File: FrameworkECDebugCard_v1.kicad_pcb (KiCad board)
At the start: 2 copper layers, 26 x 30 mm, 25 parts, among them J1 Conn_01x05, P1 USB_C_Plug_USB2.0, P2 USB_B_Micro, U1 FT230XS

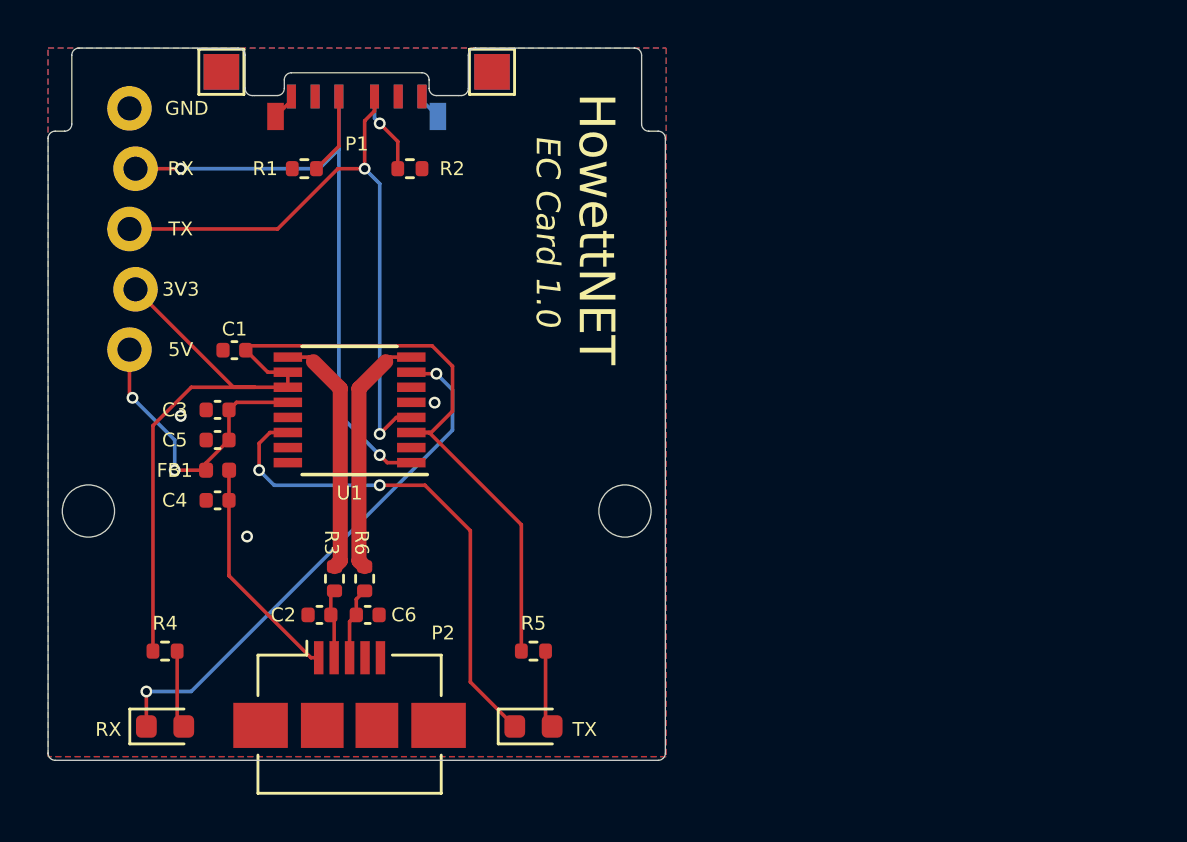
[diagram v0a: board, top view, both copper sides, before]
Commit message: Re-route everything to avoid B.Cu cuts across diff pair
Switched the positions of the TX and RX LEDs to match which side of the
chip they're on. Significantly re-routed TX/RX. Added via stitching.

The ground planes are much more contiguous, except for U1 pad 5 which
connects to GND on the back with a via.

(Kieran's suggestion was to remove the lines on the back that cut
horizontally across the differential pair; I don't know if having
RXLED's sink next to the diff pair will be a problem.)

Re-version the card to "EC Card 2"
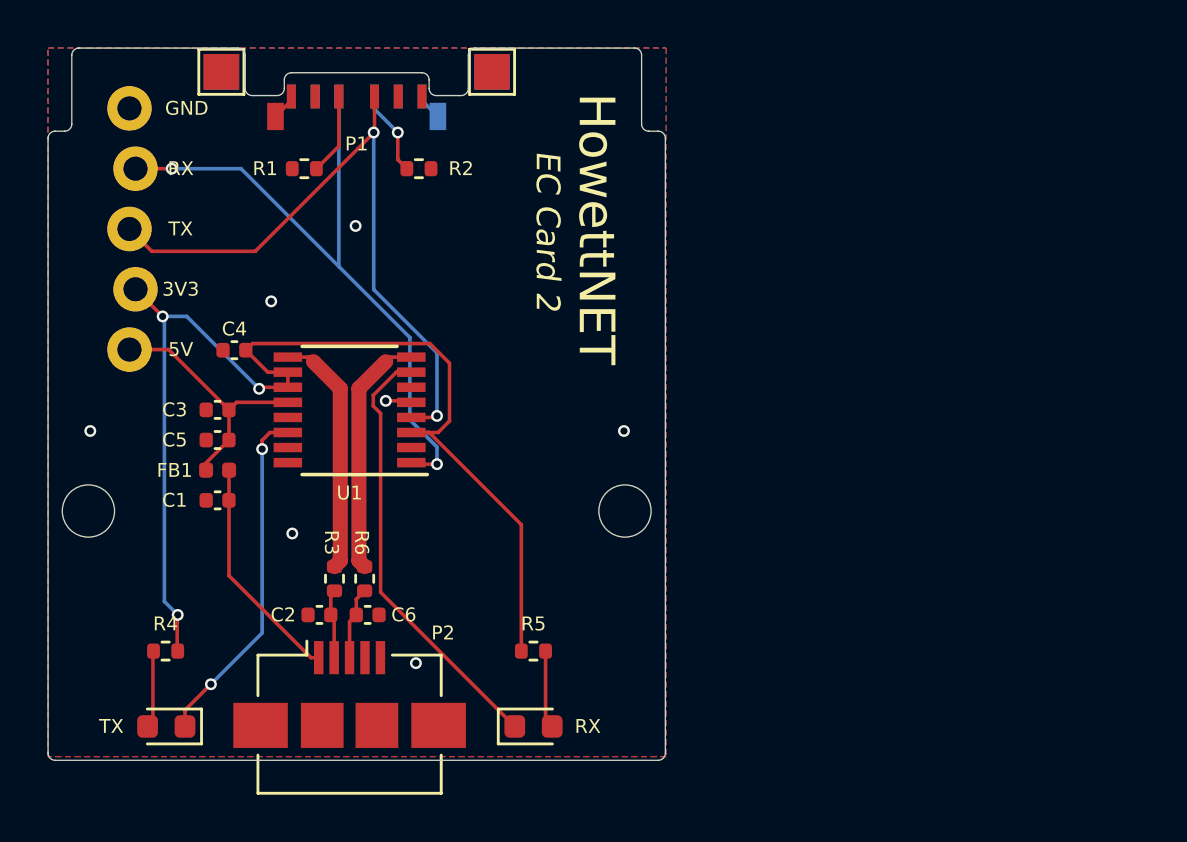
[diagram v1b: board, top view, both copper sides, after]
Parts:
- moved D2 15.5 mm to (147.4, 155.6)
- moved R5 15.5 mm to (147.4, 152.4)
- moved R4 15.5 mm to (132.0, 152.4), turned to 180 degrees
- moved D1 15.5 mm to (132.0, 155.6), turned to 180 degrees
- moved R2 0.38 mm to (142.6, 132.1)
- renumbered C4 to C1, C1 to C4, D2 to D1, D1 to D2, R5 to R4, R4 to R5
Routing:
- net /TXLED: track 21.5 -> 14.6 mm
- net /RXLED: track 22.7 -> 18.4 mm, vias 2 -> 0
- net /DIN: track 26.2 -> 28.6 mm
- net VBUS_HOST: track 12.7 -> 10.8 mm, vias 2 -> 0
- net /DOUT: track 27.2 -> 28.4 mm
- net GND: track 2.24 -> 3.34 mm, vias 3 -> 7
- net VCCIO: track 50.1 -> 50.2 mm, vias 0 -> 3
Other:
- board text added: "EC Card 2"
- board text removed: "EC Card 1.0"

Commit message: Add more stitching vias
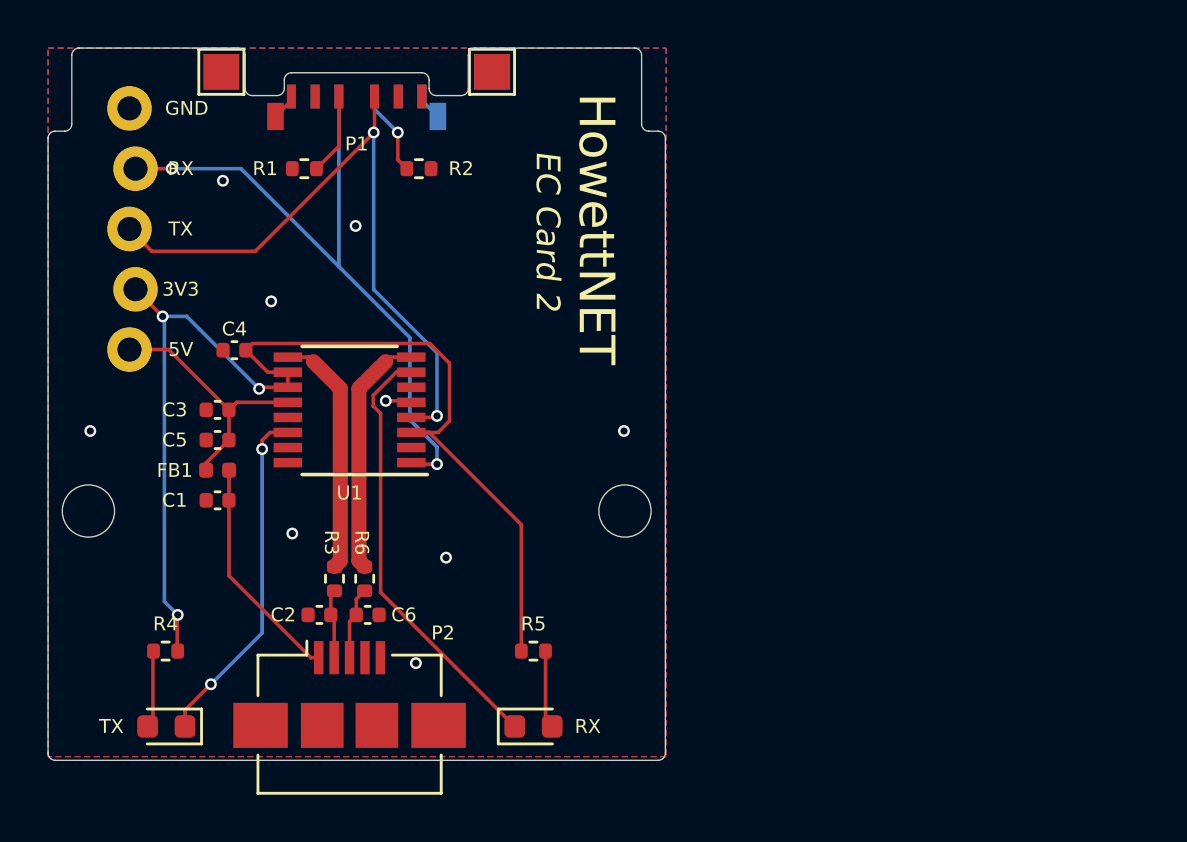
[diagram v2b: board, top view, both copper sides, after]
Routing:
- net GND: vias 7 -> 9
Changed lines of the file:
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@@
   (via (at 142.494 152.908) (size 0.5) (drill 0.3) (layers "F.Cu" "B.Cu") (free) (net 1))
   (via (at 128.778 143.129) (size 0.5) (drill 0.3) (layers "F.Cu" "B.Cu") (free) (net 1))
+  (via (at 134.366 132.588) (size 0.5) (drill 0.3) (layers "F.Cu" "B.Cu") (free) (net 1))
   (via (at 141.224 141.859) (size 0.5) (drill 0.3) (layers "F.Cu" "B.Cu") (free) (net 1))
+  (via (at 143.764 148.463) (size 0.5) (drill 0.3) (layers "F.Cu" "B.Cu") (free) (net 1))
   (via (at 139.954 134.493) (size 0.5) (drill 0.3) (layers "F.Cu" "B.Cu") (free) (net 1))
   (via (at 136.398 137.668) (size 0.5) (drill 0.3) (layers "F.Cu" "B.Cu") (free) (net 1))

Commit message: Update to KiCad 8, use narrower pads on USB C plug (PCBWay may mfg this)
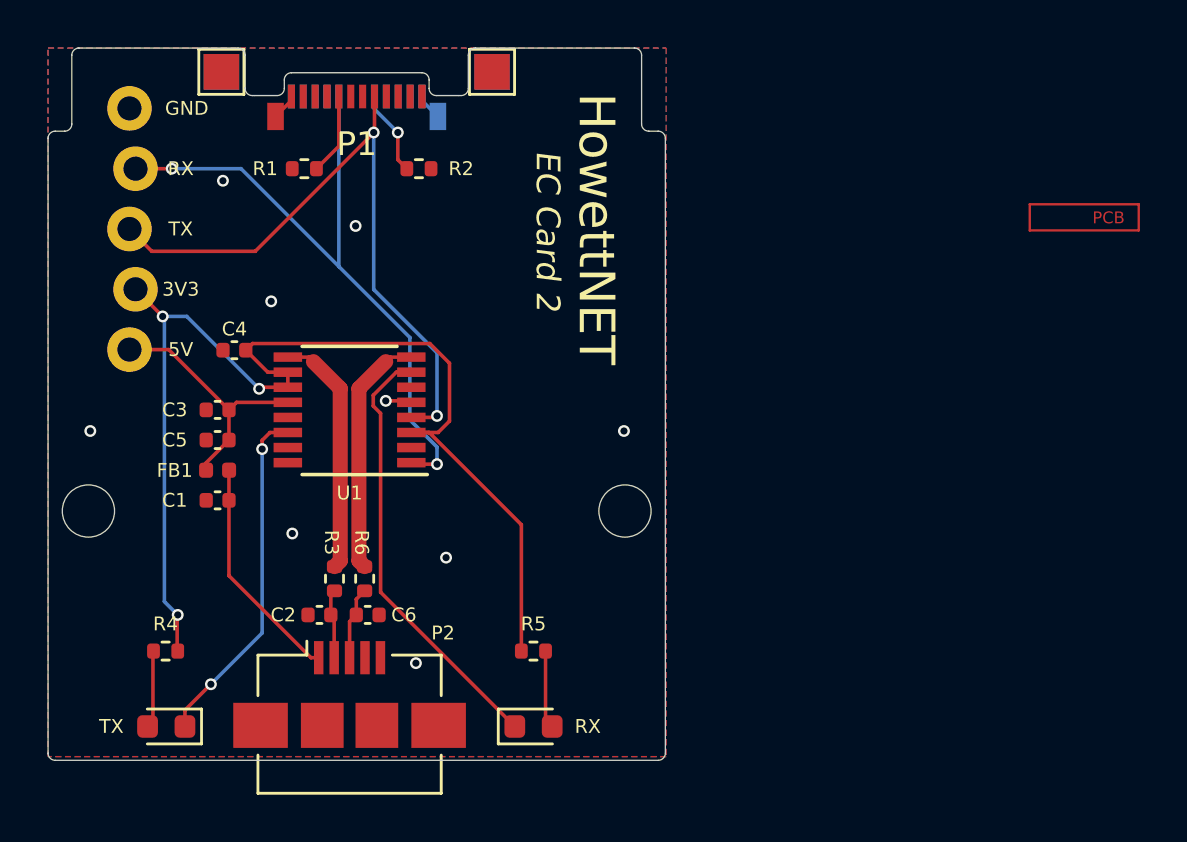
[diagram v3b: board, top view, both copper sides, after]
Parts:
- P1: footprint FrameworkECDebugCard_v1:USB_C_Plug_Molex_105444 -> FrameworkECDebugCard_v1:USB_C_Plug_Molex_105444_SmallPads
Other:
- board text added: "BOTTOM"
- board text added: "MOLEX 105444"
- board text added: "MOLEX 105444 1"
- board text added: "NC"
- board text added: "PCB"
- board text added: "TOP"

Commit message: ec card 3: recessed mid-mount usb c receptacle, fully rerouted
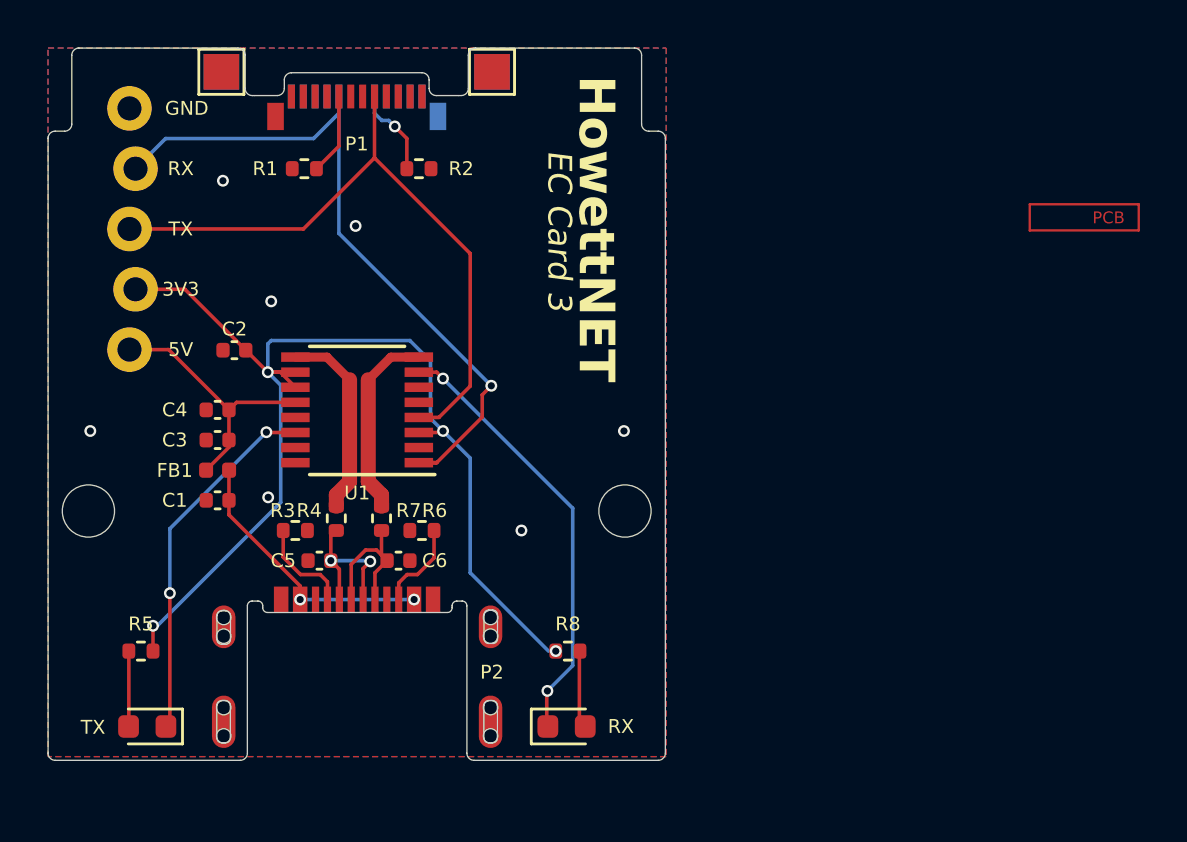
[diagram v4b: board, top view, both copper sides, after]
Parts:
- added ?: , , F.Cu at (145.6, 153.5)
- added R3: 5.1k, Resistor_SMD:R_0402_1005Metric, F.Cu at (137.4, 147.3)
- added R6: 5.1k, Resistor_SMD:R_0402_1005Metric, F.Cu at (142.7, 147.3)
- P1: value USB_C_Plug_USB2.0 -> 1054440011
- P2: value USB_B_Micro -> 2169900001; footprint Connector_USB:USB_Micro-B_Amphenol_10104110_Horizontal -> FrameworkECDebugCard_v1:USB4510-03-1-A_GCT
- moved R7 2.64 mm to (141.0, 146.8)
- moved C6 2.63 mm to (141.8, 148.6)
- moved R4 2.54 mm to (139.1, 146.8)
- moved C5 2.29 mm to (138.4, 148.6)
- moved R8 1.45 mm to (148.9, 152.4)
- moved D2 1.39 mm to (148.8, 155.6)
- moved R5 1.04 mm to (130.9, 152.4)
- moved D1 0.80 mm to (131.2, 155.6)
- moved P2 0.32 mm to (140.0, 154.2)
- moved U1 0.32 mm to (140.0, 142.2)
- renumbered C4 to C2, C5 to C3, C3 to C4, C2 to C5, R3 to R4, R4 to R5, R6 to R7, R5 to R8
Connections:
- C1 pad 1: Net-(C4-Pad1) -> Net-(C1-Pad1)
- FB1 pad 1: Net-(C4-Pad1) -> Net-(C1-Pad1)
- P1 pad A4: (no net) -> Net-(P1-VBUS-PadA4)
- P1 pad A6: (no net) -> unconnected-(P1-D+-PadA6)
- P1 pad A7: (no net) -> unconnected-(P1-D--PadA7)
- P1 pad A9: (no net) -> Net-(P1-VBUS-PadA4)
- P1 pad B4: (no net) -> Net-(P1-VBUS-PadA4)
- P1 pad B9: (no net) -> Net-(P1-VBUS-PadA4)
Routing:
- net Net-(C1-Pad1): track 0.00 -> 11.5 mm, vias 0 -> 2
- net Net-(C4-Pad1): track 9.66 -> 0.00 mm
- net Net-(P2-CC1): track 0.00 -> 4.17 mm
- net Net-(P2-CC2): track 0.00 -> 3.78 mm
- net /USBD-: track 2.94 -> 6.56 mm, vias 0 -> 2
- net /USBD+: track 3.08 -> 6.64 mm
- net GND: track 3.34 -> 0.34 mm, vias 9 -> 7
- net VCCIO: track 50.2 -> 47.7 mm, vias 3 -> 4
- net /F_USBD+: track 10.4 -> 8.09 mm
- net /DIN: track 28.6 -> 30.8 mm, vias 2 -> 1
- net /F_USBD-: track 10.4 -> 8.24 mm
- net /TXLED: track 14.6 -> 15.4 mm
- net /DOUT: track 28.4 -> 28.1 mm, vias 2 -> 0
- net /RXLED: track 18.4 -> 18.6 mm, vias 0 -> 2
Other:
- outline, holes or cut-outs redrawn
- board text added: "EC Card 3"
- board text removed: "EC Card 2"

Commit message: ec3: rebuild the pcb to the same shape as the usb c card; not routed
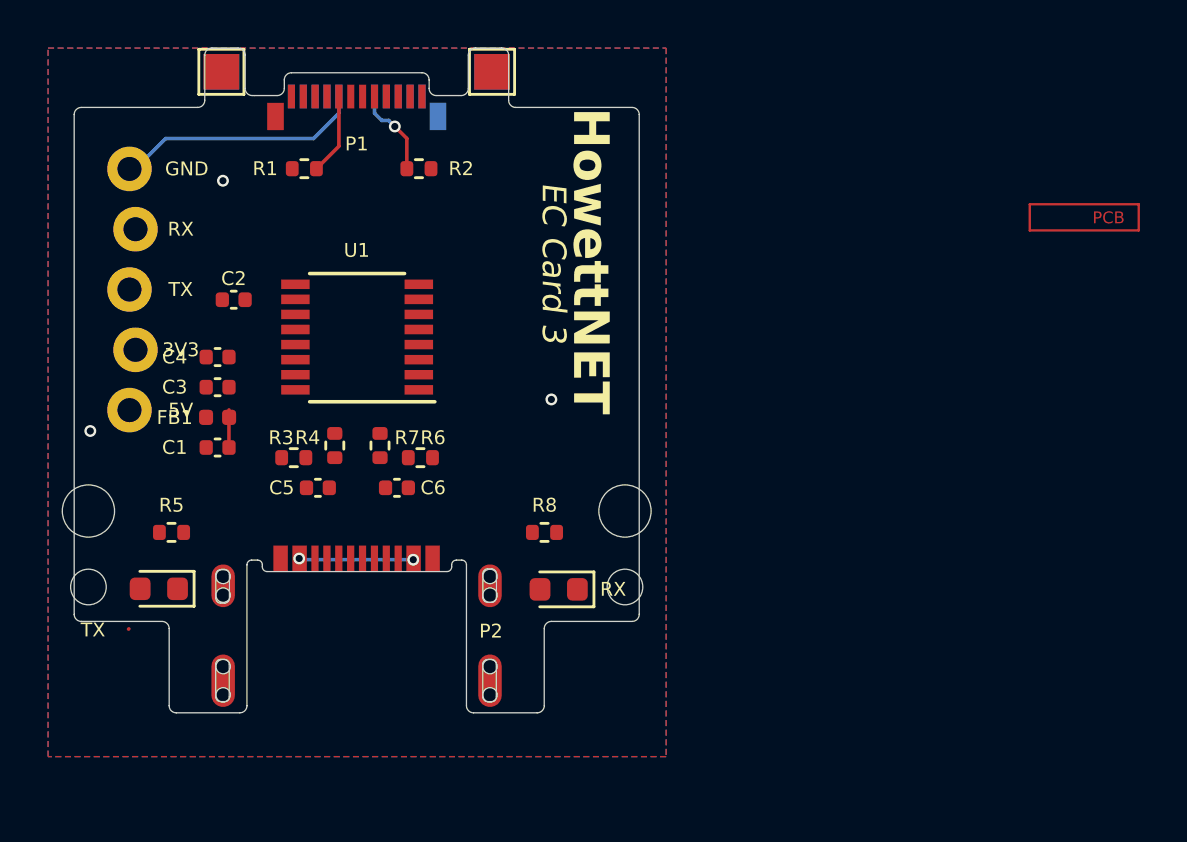
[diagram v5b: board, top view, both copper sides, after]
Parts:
- added H3: MountingHole, FrameworkECDebugCard_v1:MountingHole_1.5mm_NPTH, F.Cu at (128.7, 149.7)
- added H4: MountingHole, FrameworkECDebugCard_v1:MountingHole_1.5mm_NPTH, F.Cu at (151.3, 149.7)
- moved D1 5.82 mm to (131.7, 149.8)
- moved D2 5.78 mm to (148.5, 149.8), turned to 180 degrees
- moved R5 5.16 mm to (132.2, 147.4)
- moved R8 5.10 mm to (147.9, 147.4)
- moved C5 3.07 mm to (138.4, 145.5)
- moved C6 3.07 mm to (141.7, 145.5)
- moved R3 3.07 mm to (137.3, 144.3)
- moved R4 3.07 mm to (139.1, 143.7)
- moved R6 3.07 mm to (142.7, 144.3)
- moved R7 3.07 mm to (141.0, 143.7)
- moved U1 3.07 mm to (140.0, 139.2)
- moved J1 2.55 mm to (130.6, 142.2)
- moved C1 2.23 mm to (134.1, 143.8)
- moved C4 2.23 mm to (134.1, 140.0)
- moved FB1 2.23 mm to (134.1, 142.6)
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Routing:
- net VCCIO: track 47.7 -> 0.00 mm, vias 4 -> 0
- net /DOUT: track 28.1 -> 0.00 mm
- net /DIN: track 30.8 -> 10.2 mm, vias 1 -> 0
- net /RXLED: track 18.6 -> 0.00 mm, vias 2 -> 0
- net /TXLED: track 15.4 -> 0.00 mm, vias 2 -> 0
- net VBUS_HOST: track 11.1 -> 0.00 mm
- net /F_USBD-: track 8.24 -> 0.00 mm
- net /F_USBD+: track 8.09 -> 0.00 mm
- net /USBD+: track 6.64 -> 0.00 mm
- net /USBD-: track 6.56 -> 0.00 mm, vias 2 -> 0
- net Net-(C1-Pad1): track 11.5 -> 6.15 mm
- net Net-(P2-CC1): track 4.17 -> 0.00 mm
- net Net-(P2-CC2): track 3.78 -> 0.00 mm
- net Net-(D2-A): track 3.19 -> 0.00 mm
- net Net-(D1-A): track 3.18 -> 0.02 mm
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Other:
- board size 26 x 30 mm -> 23.8 x 28 mm

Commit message: ec3: route it! use JLCPCB's tolerances
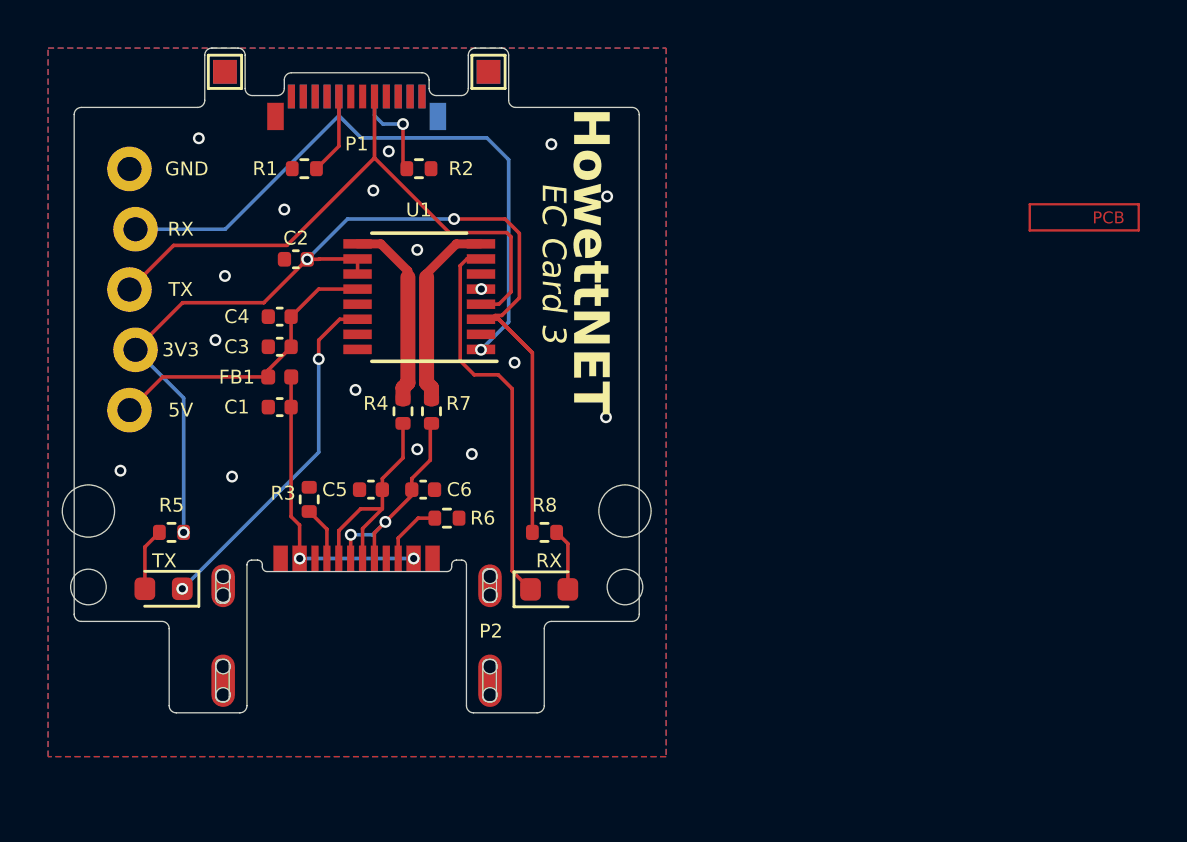
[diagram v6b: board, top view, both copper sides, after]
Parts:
- TP1, TP2, TP3, TP4: footprint TestPoint:TestPoint_Pad_1.5x1.5mm -> TestPoint:TestPoint_Pad_1.0x1.0mm
- moved R4 3.22 mm to (141.9, 142.3)
- moved C1 3.12 mm to (136.8, 142.1)
- moved C3 3.12 mm to (136.8, 139.6)
- moved C4 3.12 mm to (136.8, 138.3)
- moved C2 3.12 mm to (137.4, 135.9)
- moved FB1 3.12 mm to (136.8, 140.9)
- moved U1 3.12 mm to (142.6, 137.5)
- moved R6 2.78 mm to (143.8, 146.8), turned to 180 degrees
- moved R7 2.60 mm to (143.2, 142.3)
- moved C5 2.24 mm to (140.6, 145.6)
- moved R3 1.87 mm to (138.0, 146.0), turned to -90 degrees
- moved C6 1.11 mm to (142.8, 145.6)
- moved D2 0.40 mm to (148.1, 149.8), turned to 0 degrees
- moved D1 0.20 mm to (131.9, 149.8)
- moved TP1 0.15 mm to (134.4, 128.0)
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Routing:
- net VCCIO: track 0.00 -> 46.6 mm, vias 0 -> 3
- net /DOUT: track 0.00 -> 26.1 mm
- net /DIN: track 10.2 -> 27.8 mm, vias 0 -> 1
- net /RXLED: track 0.00 -> 16.4 mm
- net /TXLED: track 0.00 -> 14.9 mm, vias 0 -> 2
- net VBUS_HOST: track 0.00 -> 12.6 mm
- net /USBD-: track 0.00 -> 9.78 mm
- net /USBD+: track 0.00 -> 9.37 mm, vias 0 -> 2
- net /F_USBD+: track 0.00 -> 8.18 mm
- net /F_USBD-: track 0.00 -> 8.08 mm
- net Net-(C1-Pad1): track 6.15 -> 12.6 mm
- net Net-(P2-CC2): track 0.00 -> 2.75 mm
- net Net-(D1-A): track 0.02 -> 2.63 mm
- net Net-(D2-A): track 0.00 -> 2.60 mm
- net Net-(P2-CC1): track 0.00 -> 2.29 mm
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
